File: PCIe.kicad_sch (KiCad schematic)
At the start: 12 parts, among them J3001 Bus_M.2_Socket_M

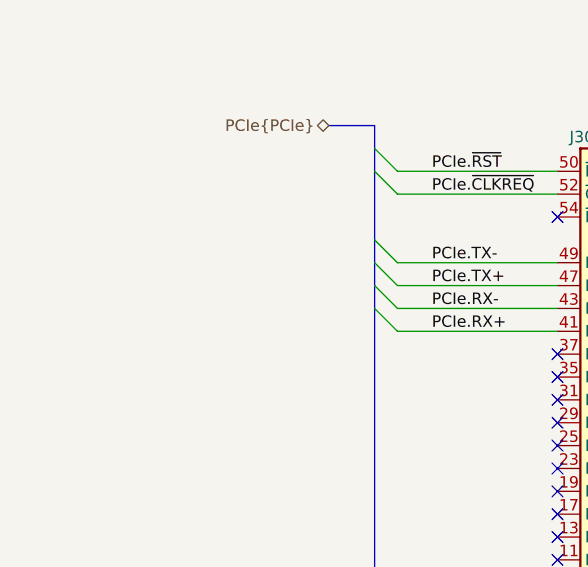
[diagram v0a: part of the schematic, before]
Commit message: Add comments about diff pair polarity
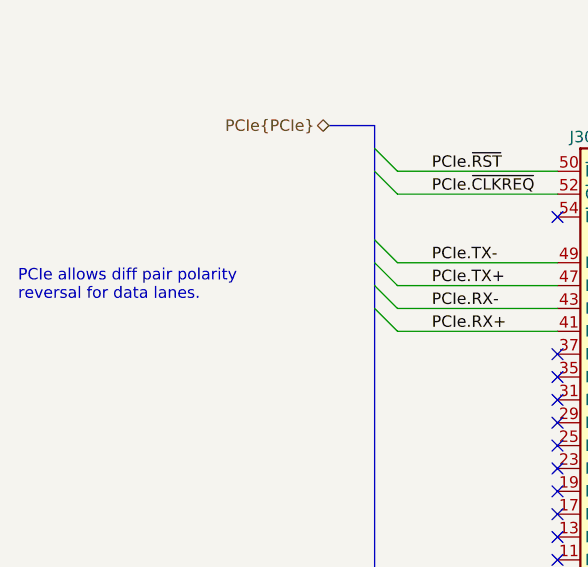
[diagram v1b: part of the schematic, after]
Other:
- note added: "PCIe allows diff pair polarity reversal for data lanes."
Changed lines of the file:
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@@
 		(comment 3 "HALPI2 is licensed under CERN-OHL-S v2.")
+	)
+	(text "PCIe allows diff pair polarity\nreversal for data lanes."
+		(exclude_from_sim no)
+		(at 28.956 60.96 0)
+		(effects
+			(font
+				(size 1.27 1.27)
+			)
+			(justify left)
+		)
 	)
 	(junction

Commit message: Reannotate the board
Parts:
- renumbered C3001 to C133, C3002 to C134, C3003 to C135, C3004 to C136, C3005 to C137, D3001 to D27, H3001 to H3, H3002 to H4, H3003 to H5, H3004 to H6, J3001 to J25, R3001 to R95
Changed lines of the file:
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@@
 		(on_board yes)
 		(dnp no)
-		(property "Reference" "C3001"
+		(property "Reference" "C133"
 			(at 121.7042 30.6006 0)
 			(effects
@@
 			(project "Yellow"
 				(path "/abc482bd-3f17-4d35-80db-1da3dcdb5c27/a1a835e0-c072-4609-9cb4-4b95bf746f54"
-					(reference "C3001")
+					(reference "C133")
 					(unit 1)
 				)
@@
 		(on_board yes)
 		(dnp no)
-		(property "Reference" "C3002"
+		(property "Reference" "C134"
 			(at 133.1342 30.6006 0)
 			(effects
@@
 			(project "Yellow"
 				(path "/abc482bd-3f17-4d35-80db-1da3dcdb5c27/a1a835e0-c072-4609-9cb4-4b95bf746f54"
-					(reference "C3002")
+					(reference "C134")
 					(unit 1)
 				)
@@
 		(on_board yes)
 		(dnp no)
-		(property "Reference" "J3001"
+		(property "Reference" "J25"
 			(at 92.71 44.45 0)
 			(effects
@@
 			(project "Yellow"
 				(path "/abc482bd-3f17-4d35-80db-1da3dcdb5c27/a1a835e0-c072-4609-9cb4-4b95bf746f54"
-					(reference "J3001")
+					(reference "J25")
 					(unit 1)
 				)
@@
 		(on_board yes)
 		(dnp no)
-		(property "Reference" "D3001"
+		(property "Reference" "D27"
 			(at 147.32 92.71 90)
 			(effects
@@
 			(project "Yellow"
 				(path "/abc482bd-3f17-4d35-80db-1da3dcdb5c27/a1a835e0-c072-4609-9cb4-4b95bf746f54"
-					(reference "D3001")
+					(reference "D27")
 					(unit 1)
 				)
@@
 		(dnp no)
 		(fields_autoplaced yes)
-		(property "Reference" "C3005"
+		(property "Reference" "C137"
 			(at 166.37 30.4862 0)
 			(effects
@@
 			(project "HALPI2"
 				(path "/abc482bd-3f17-4d35-80db-1da3dcdb5c27/a1a835e0-c072-4609-9cb4-4b95bf746f54"
-					(reference "C3005")
+					(reference "C137")
 					(unit 1)
 				)
@@
 		(on_board yes)
 		(dnp no)
-		(property "Reference" "#PWR03002"
+		(property "Reference" "#PWR0241"
 			(at 102.87 175.26 0)
 			(effects
@@
 			(project "HALPI2"
 				(path "/abc482bd-3f17-4d35-80db-1da3dcdb5c27/a1a835e0-c072-4609-9cb4-4b95bf746f54"
-					(reference "#PWR03002")
+					(reference "#PWR0241")
 					(unit 1)
 				)
@@
 		(dnp no)
 		(fields_autoplaced yes)
-		(property "Reference" "H3001"
+		(property "Reference" "H3"
 			(at 86.614 162.5599 0)
 			(effects
@@
 			(project "HALPI2"
 				(path "/abc482bd-3f17-4d35-80db-1da3dcdb5c27/a1a835e0-c072-4609-9cb4-4b95bf746f54"
-					(reference "H3001")
+					(reference "H3")
 					(unit 1)
 				)
@@
 		(dnp no)
 		(fields_autoplaced yes)
-		(property "Reference" "H3004"
+		(property "Reference" "H6"
 			(at 143.764 162.5599 0)
 			(effects
@@
 			(project "HALPI2"
 				(path "/abc482bd-3f17-4d35-80db-1da3dcdb5c27/a1a835e0-c072-4609-9cb4-4b95bf746f54"
-					(reference "H3004")
+					(reference "H6")
 					(unit 1)
 				)
@@
 		(on_board yes)
 		(dnp no)
-		(property "Reference" "C3003"
+		(property "Reference" "C135"
 			(at 143.2942 30.6006 0)
 			(effects
@@
 			(project "Yellow"
 				(path "/abc482bd-3f17-4d35-80db-1da3dcdb5c27/a1a835e0-c072-4609-9cb4-4b95bf746f54"
-					(reference "C3003")
+					(reference "C135")
 					(unit 1)
 				)
@@
 		(dnp no)
 		(fields_autoplaced yes)
-		(property "Reference" "#PWR03008"
+		(property "Reference" "#PWR0247"
 			(at 144.78 80.01 0)
 			(effects
@@
 			(project "HALPI2"
 				(path "/abc482bd-3f17-4d35-80db-1da3dcdb5c27/a1a835e0-c072-4609-9cb4-4b95bf746f54"
-					(reference "#PWR03008")
+					(reference "#PWR0247")
 					(unit 1)
 				)
@@
 		(dnp no)
 		(fields_autoplaced yes)
-		(property "Reference" "#PWR03003"
+		(property "Reference" "#PWR0242"
 			(at 114.3 30.48 0)
 			(effects
@@
 			(project ""
 				(path "/abc482bd-3f17-4d35-80db-1da3dcdb5c27/a1a835e0-c072-4609-9cb4-4b95bf746f54"
-					(reference "#PWR03003")
+					(reference "#PWR0242")
 					(unit 1)
 				)
@@
 		(on_board yes)
 		(dnp no)
-		(property "Reference" "R3001"
+		(property "Reference" "R95"
 			(at 147.32 82.55 0)
 			(effects
@@
 			(project "Yellow"
 				(path "/abc482bd-3f17-4d35-80db-1da3dcdb5c27/a1a835e0-c072-4609-9cb4-4b95bf746f54"
-					(reference "R3001")
+					(reference "R95")
 					(unit 1)
 				)
@@
 		(on_board yes)
 		(dnp no)
-		(property "Reference" "#PWR03006"
+		(property "Reference" "#PWR0245"
 			(at 140.97 43.18 0)
 			(effects
@@
 			(project "Yellow"
 				(path "/abc482bd-3f17-4d35-80db-1da3dcdb5c27/a1a835e0-c072-4609-9cb4-4b95bf746f54"
-					(reference "#PWR03006")
+					(reference "#PWR0245")
 					(unit 1)
 				)
@@
 		(dnp no)
 		(fields_autoplaced yes)
-		(property "Reference" "H3002"
+		(property "Reference" "H4"
 			(at 105.664 162.5599 0)
 			(effects
@@
 			(project "HALPI2"
 				(path "/abc482bd-3f17-4d35-80db-1da3dcdb5c27/a1a835e0-c072-4609-9cb4-4b95bf746f54"
-					(reference "H3002")
+					(reference "H4")
 					(unit 1)
 				)
@@
 		(on_board yes)
 		(dnp no)
-		(property "Reference" "#PWR03007"
+		(property "Reference" "#PWR0246"
 			(at 140.97 175.26 0)
 			(effects
@@
 			(project "HALPI2"
 				(path "/abc482bd-3f17-4d35-80db-1da3dcdb5c27/a1a835e0-c072-4609-9cb4-4b95bf746f54"
-					(reference "#PWR03007")
+					(reference "#PWR0246")
 					(unit 1)
 				)
@@
 		(dnp no)
 		(fields_autoplaced yes)
-		(property "Reference" "H3003"
+		(property "Reference" "H5"
 			(at 124.714 162.5599 0)
 			(effects
@@
 			(project "HALPI2"
 				(path "/abc482bd-3f17-4d35-80db-1da3dcdb5c27/a1a835e0-c072-4609-9cb4-4b95bf746f54"
-					(reference "H3003")
+					(reference "H5")
 					(unit 1)
 				)
@@
 		(on_board yes)
 		(dnp no)
-		(property "Reference" "#PWR03005"
+		(property "Reference" "#PWR0244"
 			(at 121.92 175.26 0)
 			(effects
@@
 			(project "HALPI2"
 				(path "/abc482bd-3f17-4d35-80db-1da3dcdb5c27/a1a835e0-c072-4609-9cb4-4b95bf746f54"
-					(reference "#PWR03005")
+					(reference "#PWR0244")
 					(unit 1)
 				)
@@
 		(on_board yes)
 		(dnp no)
-		(property "Reference" "#PWR03001"
+		(property "Reference" "#PWR0240"
 			(at 83.82 175.26 0)
 			(effects
@@
 			(project "HALPI2"
 				(path "/abc482bd-3f17-4d35-80db-1da3dcdb5c27/a1a835e0-c072-4609-9cb4-4b95bf746f54"
-					(reference "#PWR03001")
+					(reference "#PWR0240")
 					(unit 1)
 				)
@@
 		(dnp no)
 		(fields_autoplaced yes)
-		(property "Reference" "C3004"
+		(property "Reference" "C136"
 			(at 154.94 30.4862 0)
 			(effects
@@
 			(project "HALPI2"
 				(path "/abc482bd-3f17-4d35-80db-1da3dcdb5c27/a1a835e0-c072-4609-9cb4-4b95bf746f54"
-					(reference "C3004")
+					(reference "C136")
 					(unit 1)
 				)
@@
 		(on_board yes)
 		(dnp no)
-		(property "Reference" "#PWR03004"
+		(property "Reference" "#PWR0243"
 			(at 114.3 148.59 0)
 			(effects
@@
 			(project "Yellow"
 				(path "/abc482bd-3f17-4d35-80db-1da3dcdb5c27/a1a835e0-c072-4609-9cb4-4b95bf746f54"
-					(reference "#PWR03004")
-					(unit 1)
-				)
+					(reference "#PWR0243")
+					(unit 1)
+				)

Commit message: FInal v0.2.0 proto changes
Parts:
- J25: JLCPCB_CORRECTION (none) -> 0;-1.5;0
- renumbered C133 to C135, C134 to C136, C135 to C137, C136 to C138, C137 to C139
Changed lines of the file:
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@@
 		(on_board yes)
 		(dnp no)
-		(property "Reference" "C133"
+		(property "Reference" "C135"
 			(at 121.7042 30.6006 0)
 			(effects
@@
 			(project "Yellow"
 				(path "/abc482bd-3f17-4d35-80db-1da3dcdb5c27/a1a835e0-c072-4609-9cb4-4b95bf746f54"
-					(reference "C133")
+					(reference "C135")
 					(unit 1)
 				)
@@
 		(on_board yes)
 		(dnp no)
-		(property "Reference" "C134"
+		(property "Reference" "C136"
 			(at 133.1342 30.6006 0)
 			(effects
@@
 			(project "Yellow"
 				(path "/abc482bd-3f17-4d35-80db-1da3dcdb5c27/a1a835e0-c072-4609-9cb4-4b95bf746f54"
-					(reference "C134")
+					(reference "C136")
 					(unit 1)
 				)
@@
 			)
 		)
-		(property "Field8" ""
-			(at 114.3 91.44 0)
-			(effects
-				(font
-					(size 1.27 1.27)
-				)
-			)
-		)
 		(property "PartNumber" ""
 			(at 114.3 91.44 0)
@@
 		)
 		(property "Sim.Enable" ""
+			(at 114.3 91.44 0)
+			(effects
+				(font
+					(size 1.27 1.27)
+				)
+			)
+		)
+		(property "JLCPCB_CORRECTION" "0;-1.5;0"
 			(at 114.3 91.44 0)
 			(effects
@@
 		(dnp no)
 		(fields_autoplaced yes)
-		(property "Reference" "C137"
+		(property "Reference" "C139"
 			(at 166.37 30.4862 0)
 			(effects
@@
 			(project "HALPI2"
 				(path "/abc482bd-3f17-4d35-80db-1da3dcdb5c27/a1a835e0-c072-4609-9cb4-4b95bf746f54"
-					(reference "C137")
+					(reference "C139")
 					(unit 1)
 				)
@@
 		(on_board yes)
 		(dnp no)
-		(property "Reference" "#PWR0241"
+		(property "Reference" "#PWR0242"
 			(at 102.87 175.26 0)
 			(effects
@@
 			(project "HALPI2"
 				(path "/abc482bd-3f17-4d35-80db-1da3dcdb5c27/a1a835e0-c072-4609-9cb4-4b95bf746f54"
-					(reference "#PWR0241")
+					(reference "#PWR0242")
 					(unit 1)
 				)
@@
 		(on_board yes)
 		(dnp no)
-		(property "Reference" "C135"
+		(property "Reference" "C137"
 			(at 143.2942 30.6006 0)
 			(effects
@@
 			(project "Yellow"
 				(path "/abc482bd-3f17-4d35-80db-1da3dcdb5c27/a1a835e0-c072-4609-9cb4-4b95bf746f54"
-					(reference "C135")
+					(reference "C137")
 					(unit 1)
 				)
@@
 		(dnp no)
 		(fields_autoplaced yes)
-		(property "Reference" "#PWR0247"
+		(property "Reference" "#PWR0248"
 			(at 144.78 80.01 0)
 			(effects
@@
 			(project "HALPI2"
 				(path "/abc482bd-3f17-4d35-80db-1da3dcdb5c27/a1a835e0-c072-4609-9cb4-4b95bf746f54"
-					(reference "#PWR0247")
+					(reference "#PWR0248")
 					(unit 1)
 				)
@@
 		(dnp no)
 		(fields_autoplaced yes)
-		(property "Reference" "#PWR0242"
+		(property "Reference" "#PWR0243"
 			(at 114.3 30.48 0)
 			(effects
@@
 			(project ""
 				(path "/abc482bd-3f17-4d35-80db-1da3dcdb5c27/a1a835e0-c072-4609-9cb4-4b95bf746f54"
-					(reference "#PWR0242")
+					(reference "#PWR0243")
 					(unit 1)
 				)
@@
 		(on_board yes)
 		(dnp no)
-		(property "Reference" "#PWR0245"
+		(property "Reference" "#PWR0246"
 			(at 140.97 43.18 0)
 			(effects
@@
 			(project "Yellow"
 				(path "/abc482bd-3f17-4d35-80db-1da3dcdb5c27/a1a835e0-c072-4609-9cb4-4b95bf746f54"
-					(reference "#PWR0245")
+					(reference "#PWR0246")
 					(unit 1)
 				)
@@
 		(on_board yes)
 		(dnp no)
-		(property "Reference" "#PWR0246"
+		(property "Reference" "#PWR0247"
 			(at 140.97 175.26 0)
 			(effects
@@
 			(project "HALPI2"
 				(path "/abc482bd-3f17-4d35-80db-1da3dcdb5c27/a1a835e0-c072-4609-9cb4-4b95bf746f54"
-					(reference "#PWR0246")
+					(reference "#PWR0247")
 					(unit 1)
 				)
@@
 		(on_board yes)
 		(dnp no)
-		(property "Reference" "#PWR0244"
+		(property "Reference" "#PWR0245"
 			(at 121.92 175.26 0)
 			(effects
@@
 			(project "HALPI2"
 				(path "/abc482bd-3f17-4d35-80db-1da3dcdb5c27/a1a835e0-c072-4609-9cb4-4b95bf746f54"
-					(reference "#PWR0244")
+					(reference "#PWR0245")
 					(unit 1)
 				)
@@
 		(on_board yes)
 		(dnp no)
-		(property "Reference" "#PWR0240"
+		(property "Reference" "#PWR0241"
 			(at 83.82 175.26 0)
 			(effects
@@
 			(project "HALPI2"
 				(path "/abc482bd-3f17-4d35-80db-1da3dcdb5c27/a1a835e0-c072-4609-9cb4-4b95bf746f54"
-					(reference "#PWR0240")
+					(reference "#PWR0241")
 					(unit 1)
 				)
@@
 		(dnp no)
 		(fields_autoplaced yes)
-		(property "Reference" "C136"
+		(property "Reference" "C138"
 			(at 154.94 30.4862 0)
 			(effects
@@
 			(project "HALPI2"
 				(path "/abc482bd-3f17-4d35-80db-1da3dcdb5c27/a1a835e0-c072-4609-9cb4-4b95bf746f54"
-					(reference "C136")
+					(reference "C138")
 					(unit 1)
 				)
@@
 		(on_board yes)
 		(dnp no)
-		(property "Reference" "#PWR0243"
+		(property "Reference" "#PWR0244"
 			(at 114.3 148.59 0)
 			(effects
@@
 			(project "Yellow"
 				(path "/abc482bd-3f17-4d35-80db-1da3dcdb5c27/a1a835e0-c072-4609-9cb4-4b95bf746f54"
-					(reference "#PWR0243")
+					(reference "#PWR0244")
 					(unit 1)
 				)

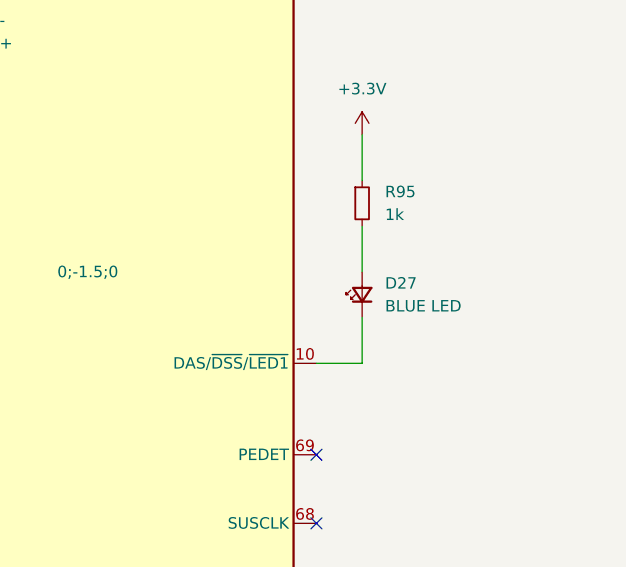
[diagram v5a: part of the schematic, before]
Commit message: Nailed the current limiter design
Also added more GND test pads
Also fixed the MCU I2C pinout
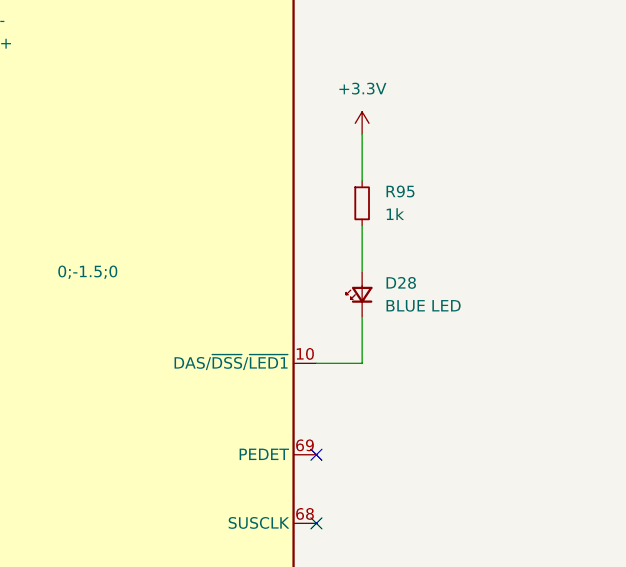
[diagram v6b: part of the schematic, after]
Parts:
- renumbered D27 to D28

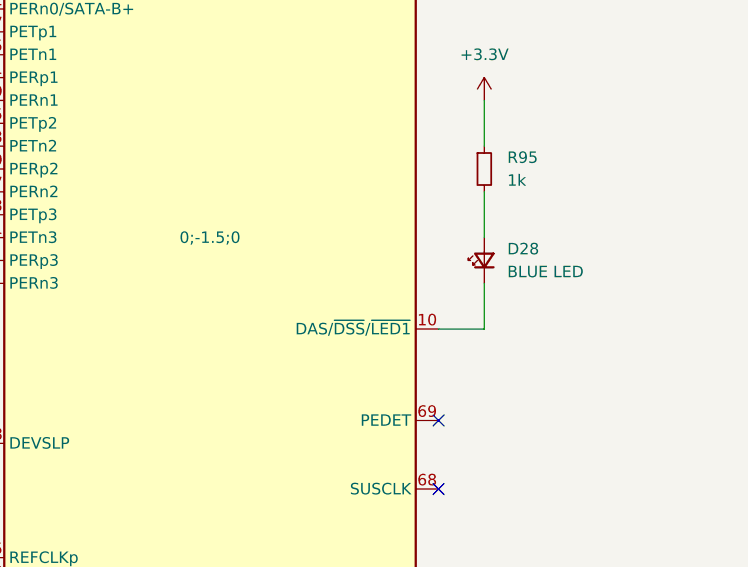
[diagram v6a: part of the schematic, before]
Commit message: Connect PCIe LED to MCU
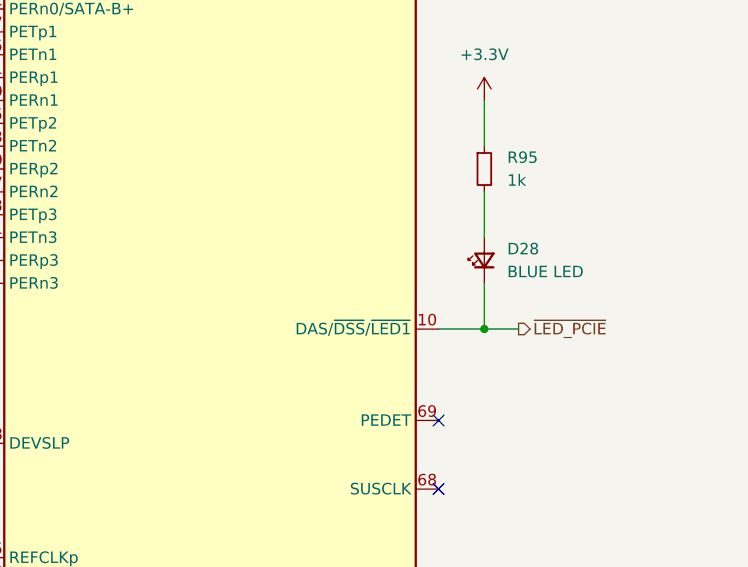
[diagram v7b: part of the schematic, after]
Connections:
- net ~{LED_PCIE}: now reaches D28.1 (K), J25.10 (DAS/~{DSS}/~{LED1})
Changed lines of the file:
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@@
+	)
+	(junction
+		(at 144.78 101.6)
+		(diameter 0)
+		(color 0 0 0 0)
 	)
 	(junction
@@
 	(wire
 		(pts
+			(xy 144.78 101.6) (xy 148.59 101.6)
+		)
+		(stroke
+			(width 0)
+			(type default)
+		)
+	)
+	(wire
+		(pts
 			(xy 152.4 34.29) (xy 152.4 35.56)
 		)
@@
 			)
 			(justify right)
+		)
+	)
+	(hierarchical_label "~{LED_PCIE}"
+		(shape output)
+		(at 148.59 101.6 0)
+		(effects
+			(font
+				(size 1.27 1.27)
+			)
+			(justify left)
+		)
+	)
+	(netclass_flag ""
+		(length 2.54)
+		(shape round)
+		(at 147.32 101.6 180)
+		(fields_autoplaced yes)
+		(effects
+			(font
+				(size 1.27 1.27)
+			)
+			(justify right bottom)
+		)
+		(property "Netclass" "Digital"
+			(at 148.209 104.14 0)
+			(effects
+				(font
+					(size 1.27 1.27)
+				)
+				(justify left)
+				(hide yes)
+			)
+		)
+		(property "Component Class" ""
+			(at -74.93 20.32 0)
+			(effects
+				(font
+					(size 1.27 1.27)
+					(italic yes)
+				)
+			)
 		)
 	)
@@
 					(size 1.27 1.27)
 				)
-			)
-		)
+				(hide yes)
+			)
+		)
